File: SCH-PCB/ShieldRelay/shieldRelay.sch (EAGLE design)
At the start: 67 parts, among them IC1 LM2596SX-5.0_NOPB, IC2 LM1117MPX-33NOPB, K1 SLA-05VDC-SL-C, K2 SRD-05VDC-SL-C, K3 G3MB-202PL-DC5, K5 G3MB-202PL-DC5, K6 SRD-05VDC-SL-C, Q1 MMST2222A-7-F, Q2 MMST2222A-7-F, Q3 MMST2222A-7-F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

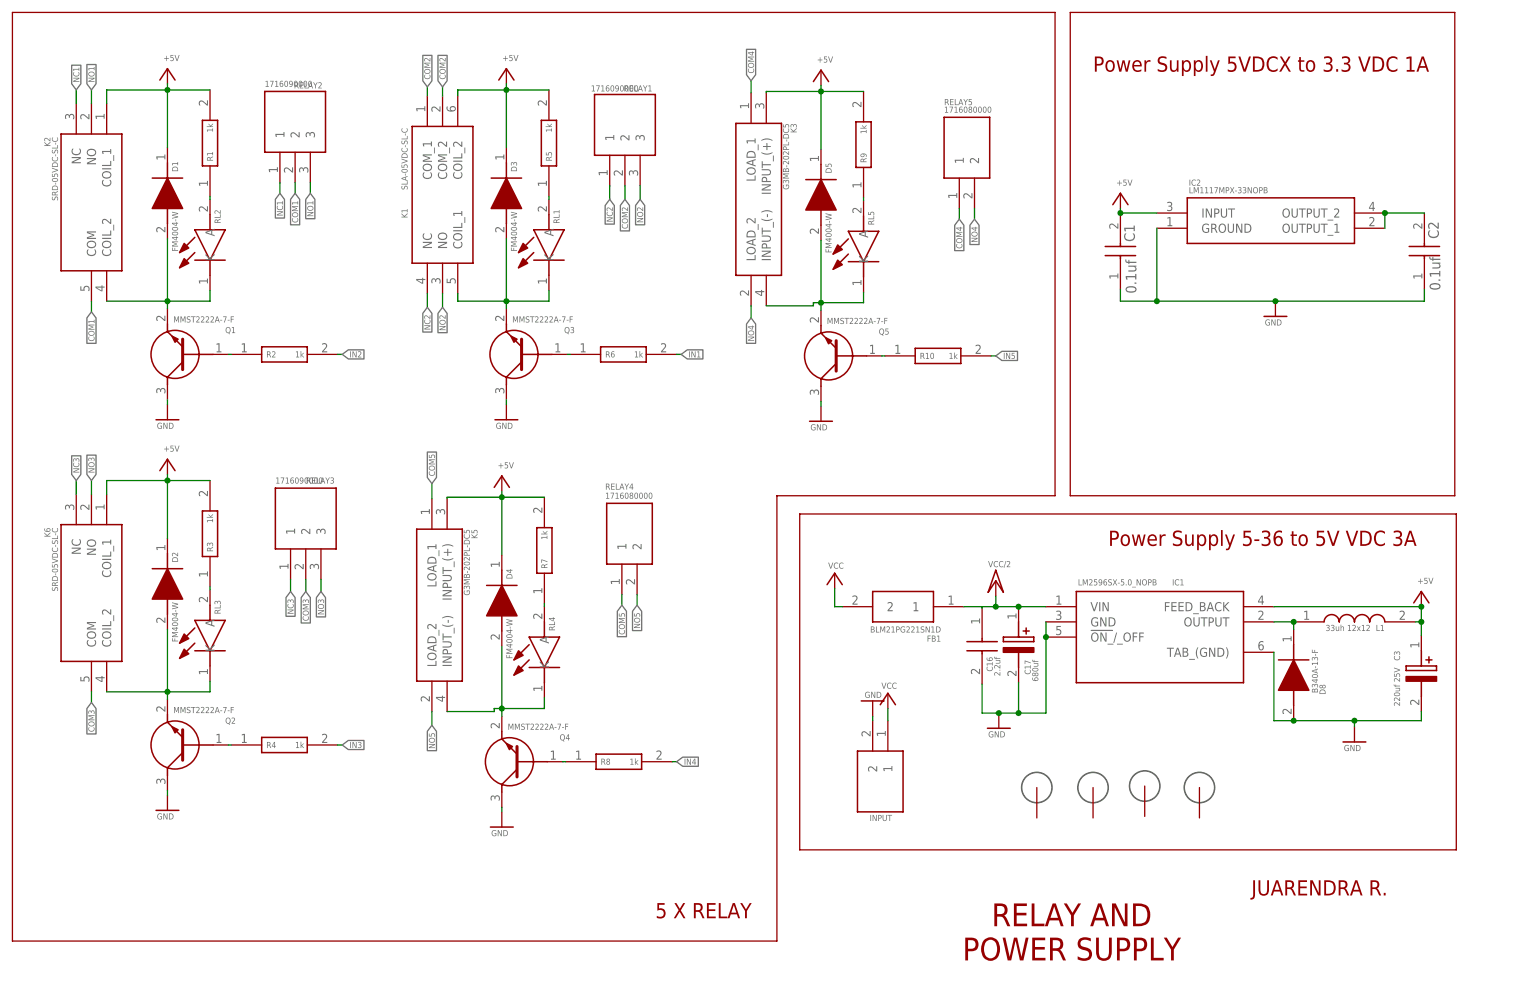
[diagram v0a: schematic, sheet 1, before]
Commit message: FIX: fix reverse transistor relay
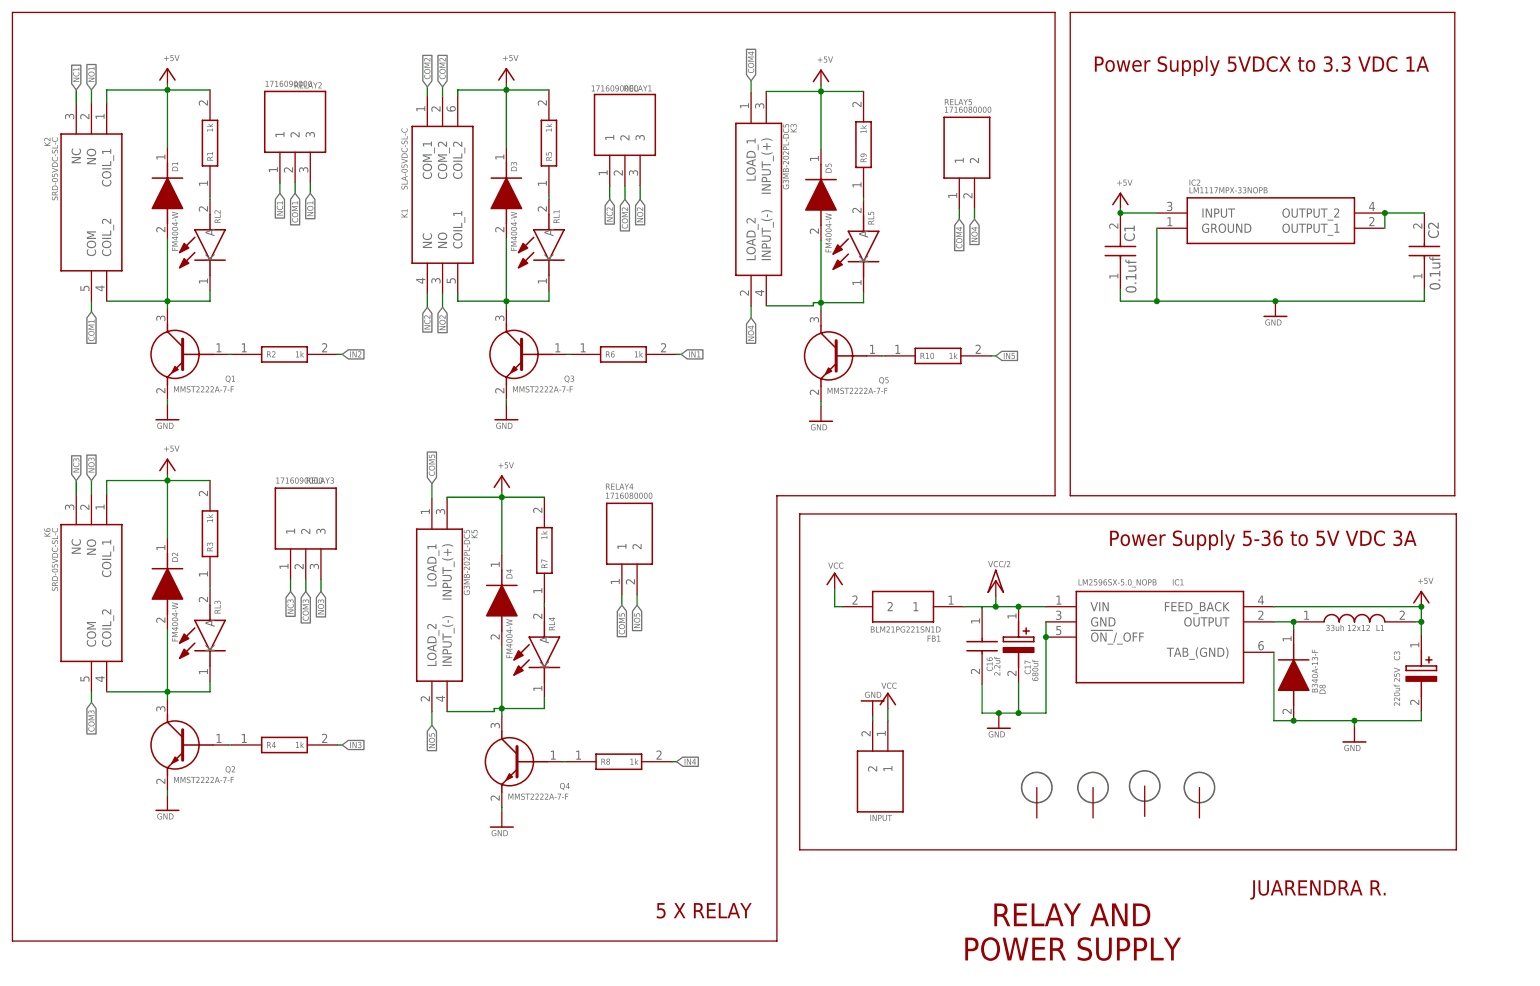
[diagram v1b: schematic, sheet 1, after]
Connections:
- net GND: now also Q1.E, Q2.E, Q3.E, Q4.E, Q5.E; no longer Q1.C, Q2.C, Q3.C, Q4.C, Q5.C
- net N$11: now also Q4.C; no longer Q4.E
- net N$14: now also Q5.C; no longer Q5.E
- net N$3: now also Q1.C; no longer Q1.E
- net N$5: now also Q2.C; no longer Q2.E
- net N$8: now also Q3.C; no longer Q3.E
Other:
- moved on the sheet: Q1, Q2, Q3, Q4, Q5
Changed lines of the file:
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@@
 <attribute name="VALUE" x="189.738" y="72.644" size="1.016" layer="96" align="center-left"/>
 </instance>
-<instance part="Q1" gate="G$1" x="47.752" y="110.744" smashed="yes" rot="R180">
-<attribute name="NAME" x="49.022" y="114.808" size="1.016" layer="95" rot="R180" align="center-left"/>
-<attribute name="VALUE" x="48.768" y="116.586" size="1.016" layer="96" rot="R180" align="center-left"/>
+<instance part="Q1" gate="G$1" x="47.752" y="110.744" smashed="yes" rot="MR0">
+<attribute name="NAME" x="49.022" y="106.68" size="1.016" layer="95" rot="MR0" align="center-left"/>
+<attribute name="VALUE" x="48.768" y="104.902" size="1.016" layer="96" rot="MR0" align="center-left"/>
 </instance>
 <instance part="RL2" gate="G$1" x="44.704" y="121.412" smashed="yes" rot="R90">
@@
 <attribute name="VALUE" x="18.796" y="81.788" size="1.016" layer="96" rot="R270" align="center-left"/>
 </instance>
-<instance part="Q2" gate="G$1" x="47.752" y="45.466" smashed="yes" rot="R180">
-<attribute name="NAME" x="49.022" y="49.53" size="1.016" layer="95" rot="R180" align="center-left"/>
-<attribute name="VALUE" x="48.768" y="51.308" size="1.016" layer="96" rot="R180" align="center-left"/>
+<instance part="Q2" gate="G$1" x="47.752" y="45.466" smashed="yes" rot="MR0">
+<attribute name="NAME" x="49.022" y="41.402" size="1.016" layer="95" rot="MR0" align="center-left"/>
+<attribute name="VALUE" x="48.768" y="39.624" size="1.016" layer="96" rot="MR0" align="center-left"/>
 </instance>
 <instance part="RL3" gate="G$1" x="44.704" y="56.134" smashed="yes" rot="R90">
@@
 <attribute name="VALUE" x="35.814" y="33.02" size="1.016" layer="96"/>
 </instance>
-<instance part="Q3" gate="G$1" x="104.394" y="110.744" smashed="yes" rot="R180">
-<attribute name="NAME" x="105.664" y="114.808" size="1.016" layer="95" rot="R180" align="center-left"/>
-<attribute name="VALUE" x="105.41" y="116.586" size="1.016" layer="96" rot="R180" align="center-left"/>
+<instance part="Q3" gate="G$1" x="104.394" y="110.744" smashed="yes" rot="MR0">
+<attribute name="NAME" x="105.664" y="106.68" size="1.016" layer="95" rot="MR0" align="center-left"/>
+<attribute name="VALUE" x="105.41" y="104.902" size="1.016" layer="96" rot="MR0" align="center-left"/>
 </instance>
 <instance part="RL1" gate="G$1" x="101.346" y="121.412" smashed="yes" rot="R90">
@@
 <attribute name="VALUE" x="92.456" y="98.298" size="1.016" layer="96"/>
 </instance>
-<instance part="Q4" gate="G$1" x="103.632" y="42.672" smashed="yes" rot="R180">
-<attribute name="NAME" x="104.902" y="46.736" size="1.016" layer="95" rot="R180" align="center-left"/>
-<attribute name="VALUE" x="104.648" y="48.514" size="1.016" layer="96" rot="R180" align="center-left"/>
+<instance part="Q4" gate="G$1" x="103.632" y="42.672" smashed="yes" rot="MR0">
+<attribute name="NAME" x="104.902" y="38.608" size="1.016" layer="95" rot="MR0" align="center-left"/>
+<attribute name="VALUE" x="104.648" y="36.83" size="1.016" layer="96" rot="MR0" align="center-left"/>
 </instance>
 <instance part="RL4" gate="G$1" x="100.584" y="53.34" smashed="yes" rot="R90">
@@
 <attribute name="VALUE" x="140.97" y="149.352" size="1.016" layer="96" rot="R270" align="center-left"/>
 </instance>
-<instance part="Q5" gate="G$1" x="156.972" y="110.49" smashed="yes" rot="R180">
-<attribute name="NAME" x="158.242" y="114.554" size="1.016" layer="95" rot="R180" align="center-left"/>
-<attribute name="VALUE" x="157.988" y="116.332" size="1.016" layer="96" rot="R180" align="center-left"/>
+<instance part="Q5" gate="G$1" x="156.972" y="110.49" smashed="yes" rot="MR0">
+<attribute name="NAME" x="158.242" y="106.426" size="1.016" layer="95" rot="MR0" align="center-left"/>
+<attribute name="VALUE" x="157.988" y="104.648" size="1.016" layer="96" rot="MR0" align="center-left"/>
 </instance>
 <instance part="RL5" gate="G$1" x="153.924" y="121.158" smashed="yes" rot="R90">
@@
 <pinref part="K2" gate="G$1" pin="COIL_2"/>
 <wire x1="27.432" y1="119.634" x2="37.592" y2="119.634" width="0.1524" layer="91"/>
-<wire x1="37.592" y1="119.634" x2="37.592" y2="130.048" width="0.1524" layer="91"/>
+<wire x1="37.592" y1="119.634" x2="37.592" y2="119.888" width="0.1524" layer="91"/>
 <pinref part="RL2" gate="G$1" pin="K"/>
+<wire x1="37.592" y1="119.888" x2="37.592" y2="130.048" width="0.1524" layer="91"/>
 <wire x1="37.592" y1="119.634" x2="44.704" y2="119.634" width="0.1524" layer="91"/>
 <wire x1="44.704" y1="119.634" x2="44.704" y2="121.412" width="0.1524" layer="91"/>
 <junction x="37.592" y="119.634"/>
-<pinref part="Q1" gate="G$1" pin="E"/>
+<pinref part="Q1" gate="G$1" pin="C"/>
 <wire x1="37.592" y1="119.634" x2="37.592" y2="118.364" width="0.1524" layer="91"/>
 </segment>
@@
 </net>
 <net name="GND" class="0">
-<segment>
-<pinref part="GND1" gate="1" pin="GND"/>
-<pinref part="Q1" gate="G$1" pin="C"/>
-<wire x1="37.592" y1="102.362" x2="37.592" y2="103.124" width="0.1524" layer="91"/>
-</segment>
-<segment>
-<pinref part="GND2" gate="1" pin="GND"/>
-<pinref part="Q2" gate="G$1" pin="C"/>
-<wire x1="37.592" y1="37.084" x2="37.592" y2="37.846" width="0.1524" layer="91"/>
-</segment>
-<segment>
-<pinref part="GND3" gate="1" pin="GND"/>
-<pinref part="Q3" gate="G$1" pin="C"/>
-<wire x1="94.234" y1="102.362" x2="94.234" y2="103.124" width="0.1524" layer="91"/>
-</segment>
-<segment>
-<pinref part="GND4" gate="1" pin="GND"/>
-<pinref part="Q4" gate="G$1" pin="C"/>
-<wire x1="93.472" y1="34.29" x2="93.472" y2="35.052" width="0.1524" layer="91"/>
-</segment>
-<segment>
-<pinref part="GND5" gate="1" pin="GND"/>
-<pinref part="Q5" gate="G$1" pin="C"/>
-<wire x1="146.812" y1="102.108" x2="146.812" y2="102.87" width="0.1524" layer="91"/>
-</segment>
 <segment>
 <pinref part="C16" gate="G$1" pin="2"/>
@@
 <junction x="202.946" y="119.634"/>
 </segment>
+<segment>
+<pinref part="Q3" gate="G$1" pin="E"/>
+<pinref part="GND3" gate="1" pin="GND"/>
+<wire x1="94.234" y1="103.124" x2="94.234" y2="102.362" width="0.1524" layer="91"/>
+</segment>
+<segment>
+<pinref part="Q1" gate="G$1" pin="E"/>
+<pinref part="GND1" gate="1" pin="GND"/>
+<wire x1="37.592" y1="103.124" x2="37.592" y2="102.362" width="0.1524" layer="91"/>
+</segment>
+<segment>
+<pinref part="Q5" gate="G$1" pin="E"/>
+<pinref part="GND5" gate="1" pin="GND"/>
+<wire x1="146.812" y1="102.87" x2="146.812" y2="102.108" width="0.1524" layer="91"/>
+</segment>
+<segment>
+<pinref part="Q4" gate="G$1" pin="E"/>
+<pinref part="GND4" gate="1" pin="GND"/>
+<wire x1="93.472" y1="35.052" x2="93.472" y2="34.29" width="0.1524" layer="91"/>
+</segment>
+<segment>
+<pinref part="Q2" gate="G$1" pin="E"/>
+<pinref part="GND2" gate="1" pin="GND"/>
+<wire x1="37.592" y1="37.846" x2="37.592" y2="37.084" width="0.1524" layer="91"/>
+</segment>
 </net>
 <net name="IN2" class="0">
@@
 <wire x1="44.704" y1="54.356" x2="44.704" y2="56.134" width="0.1524" layer="91"/>
 <junction x="37.592" y="54.356"/>
-<pinref part="Q2" gate="G$1" pin="E"/>
+<pinref part="Q2" gate="G$1" pin="C"/>
 <wire x1="37.592" y1="54.356" x2="37.592" y2="53.086" width="0.1524" layer="91"/>
 </segment>
@@
 <segment>
 <pinref part="D3" gate="G$1" pin="A"/>
-<wire x1="94.234" y1="119.634" x2="94.234" y2="130.048" width="0.1524" layer="91"/>
+<wire x1="94.234" y1="119.634" x2="94.234" y2="119.888" width="0.1524" layer="91"/>
 <pinref part="RL1" gate="G$1" pin="K"/>
+<wire x1="94.234" y1="119.888" x2="94.234" y2="130.048" width="0.1524" layer="91"/>
 <wire x1="94.234" y1="119.634" x2="101.346" y2="119.634" width="0.1524" layer="91"/>
 <wire x1="101.346" y1="119.634" x2="101.346" y2="121.412" width="0.1524" layer="91"/>
 <junction x="94.234" y="119.634"/>
-<pinref part="Q3" gate="G$1" pin="E"/>
-<wire x1="94.234" y1="119.634" x2="94.234" y2="118.364" width="0.1524" layer="91"/>
 <pinref part="K1" gate="G$1" pin="COIL_1"/>
 <wire x1="86.106" y1="120.904" x2="86.106" y2="119.634" width="0.1524" layer="91"/>
 <wire x1="86.106" y1="119.634" x2="94.234" y2="119.634" width="0.1524" layer="91"/>
+<pinref part="Q3" gate="G$1" pin="C"/>
+<wire x1="94.234" y1="119.634" x2="94.234" y2="118.364" width="0.1524" layer="91"/>
 </segment>
 </net>
@@
 <wire x1="100.584" y1="51.562" x2="100.584" y2="53.34" width="0.1524" layer="91"/>
 <junction x="93.472" y="51.562"/>
-<pinref part="Q4" gate="G$1" pin="E"/>
-<wire x1="93.472" y1="51.562" x2="93.472" y2="50.292" width="0.1524" layer="91"/>
 <pinref part="K5" gate="G$1" pin="INPUT_(-)"/>
 <wire x1="84.328" y1="51.054" x2="92.202" y2="51.054" width="0.1524" layer="91"/>
 <wire x1="92.202" y1="51.054" x2="92.202" y2="51.562" width="0.1524" layer="91"/>
 <wire x1="92.202" y1="51.562" x2="93.472" y2="51.562" width="0.1524" layer="91"/>
+<pinref part="Q4" gate="G$1" pin="C"/>
+<wire x1="93.472" y1="51.562" x2="93.472" y2="50.292" width="0.1524" layer="91"/>
 </segment>
 </net>
@@
 <wire x1="153.924" y1="119.38" x2="153.924" y2="121.158" width="0.1524" layer="91"/>
 <junction x="146.812" y="119.38"/>
-<pinref part="Q5" gate="G$1" pin="E"/>
-<wire x1="146.812" y1="119.38" x2="146.812" y2="118.11" width="0.1524" layer="91"/>
 <pinref part="K3" gate="G$1" pin="INPUT_(-)"/>
 <wire x1="137.668" y1="118.872" x2="145.542" y2="118.872" width="0.1524" layer="91"/>
 <wire x1="145.542" y1="118.872" x2="145.542" y2="119.38" width="0.1524" layer="91"/>
 <wire x1="145.542" y1="119.38" x2="146.812" y2="119.38" width="0.1524" layer="91"/>
-</segment>
-</net>
+<pinref part="Q5" gate="G$1" pin="C"/>
+<wire x1="146.812" y1="119.38" x2="146.812" y2="118.11" width="0.1524" layer="91"/>
+</segment>
+</net>
